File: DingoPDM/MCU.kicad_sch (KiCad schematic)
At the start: 39 parts, among them J4 SWD_10, SW3 SW_SPDT, U1 W25Q32JVSSIQ_TR, U11 STM32F303CCTx, U19 PCA82C250, U21 TLP172AM, Y1 8mHz, Y2 32.768kHz

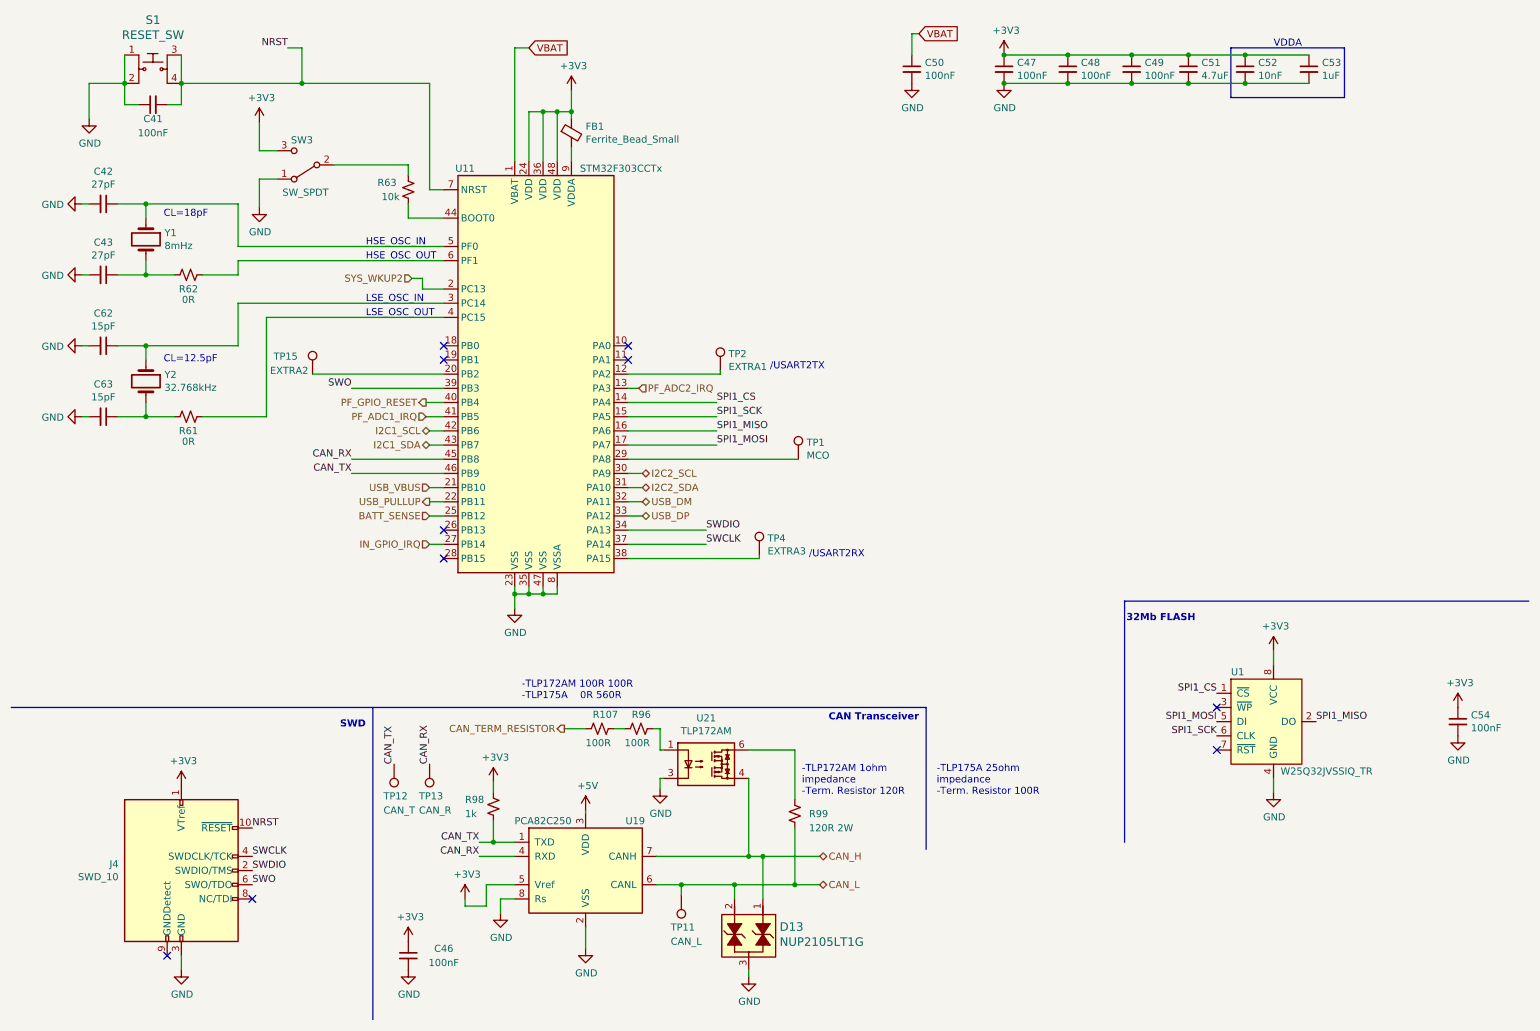
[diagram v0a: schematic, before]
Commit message: Swapped to AMPSEAL 14 pins
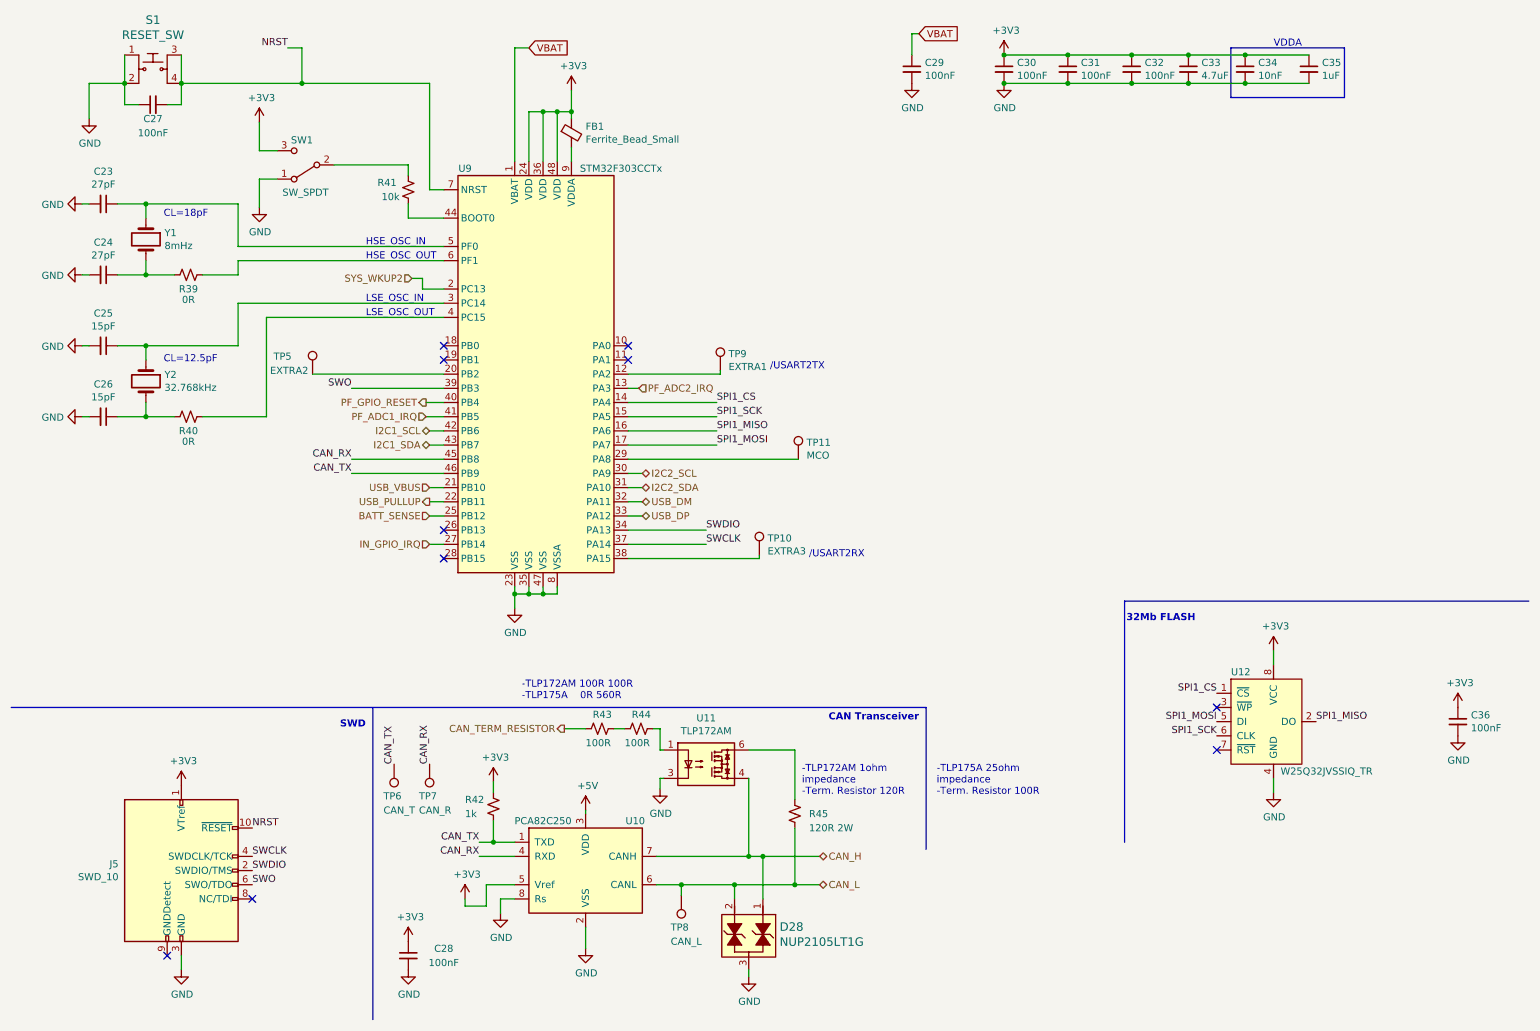
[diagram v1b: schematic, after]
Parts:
- renumbered C42 to C23, C43 to C24, C62 to C25, C63 to C26, C41 to C27, C46 to C28, C50 to C29, C47 to C30, C48 to C31, C49 to C32, C51 to C33, C52 to C34, C53 to C35, C54 to C36, D13 to D28, J4 to J5, R62 to R39, R61 to R40, R63 to R41, R98 to R42, R107 to R43, R96 to R44, R99 to R45, SW3 to SW1, TP4 to TP10, TP1 to TP11, TP15 to TP5, TP12 to TP6, TP13 to TP7, TP11 to TP8, TP2 to TP9, U19 to U10, U21 to U11, U1 to U12, U11 to U9

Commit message: Removed unused IRQs, added pd res on PF GPIO reset
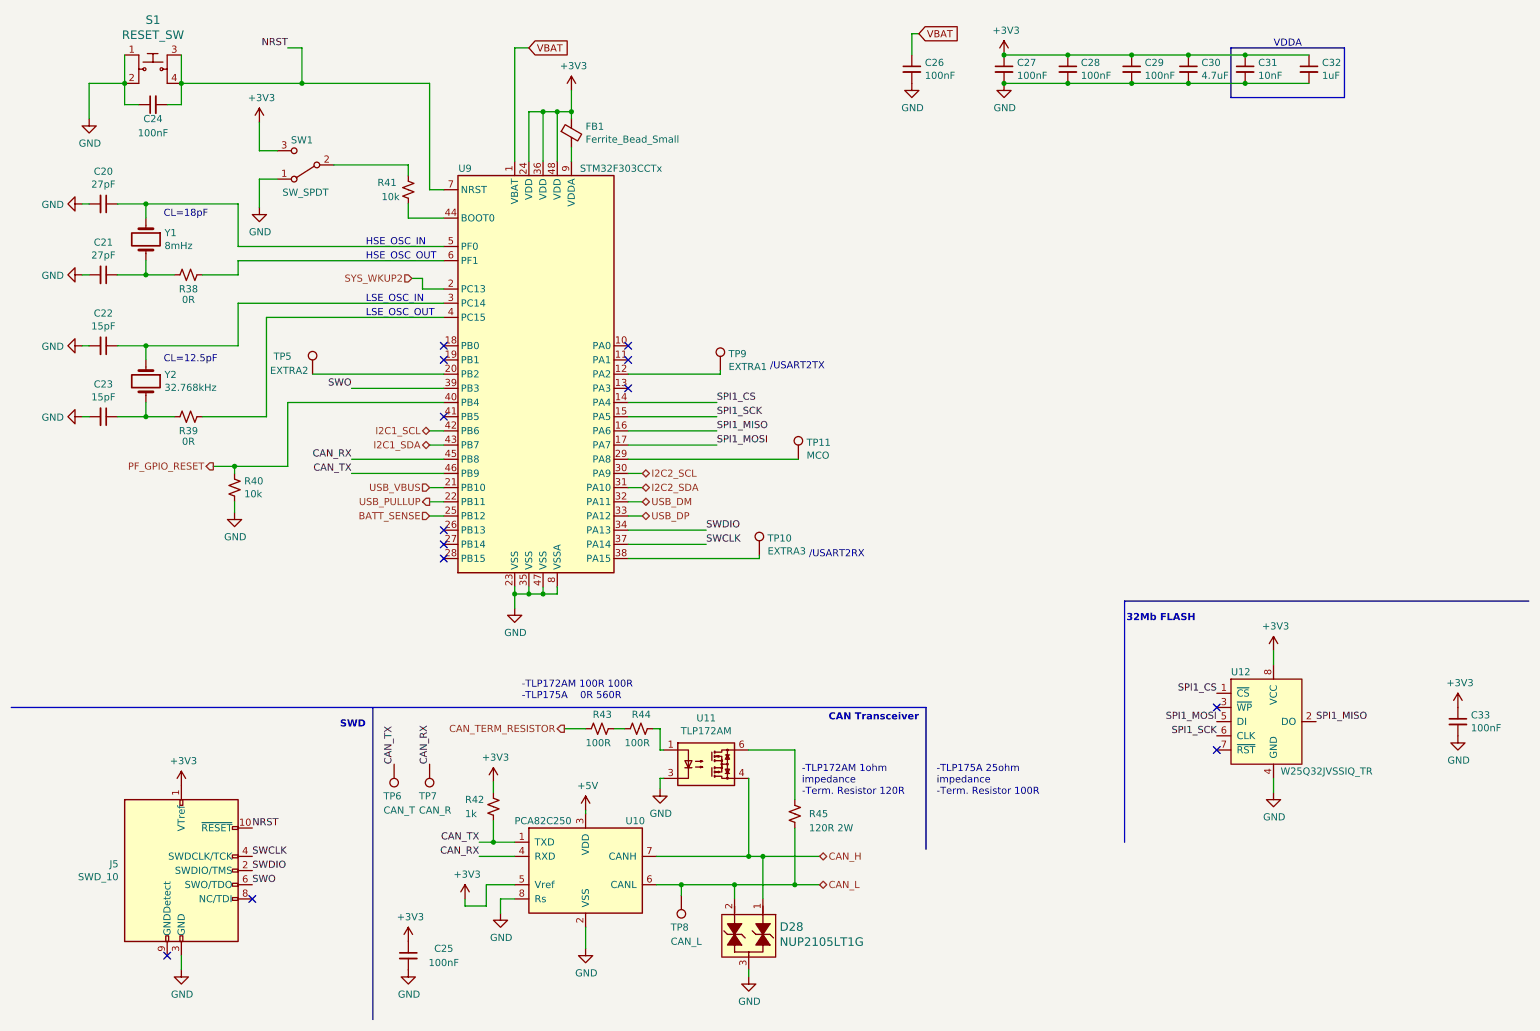
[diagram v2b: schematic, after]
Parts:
- added R40: 10k, Resistor_SMD:R_0805_2012Metric, symbol Device:R_Small_US
- renumbered C23 to C20, C24 to C21, C25 to C22, C26 to C23, C27 to C24, C28 to C25, C29 to C26, C30 to C27, C31 to C28, C32 to C29, C33 to C30, C34 to C31, C35 to C32, C36 to C33, R39 to R38, R40 to R39
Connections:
- net GND: now also R40.2
- net PF_GPIO_RESET: now also R40.1
- net IN_GPIO_IRQ: no longer names the net of U9.27 (PB14)
- net PF_ADC1_IRQ: no longer names the net of U9.41 (PB5)
- net PF_ADC2_IRQ: no longer names the net of U9.13 (PA3)
- no-connect marks 10 -> 13

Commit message: layout finished
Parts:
- removed TP8: CAN_L, TestPoint:TestPoint_Keystone_5000-5004_Miniature, symbol Connector:TestPoint
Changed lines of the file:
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@@
   (junction (at 233.68 24.13) (diameter 0) (color 0 0 0 0)
-  )
-  (junction (at 132.715 172.72) (diameter 0) (color 0 0 0 0)
   )
   (junction (at 105.41 120.65) (diameter 0) (color 0 0 0 0)
@@
     (stroke (width 0) (type default) (color 0 0 0 0))
   )
-  (wire (pts (xy 132.715 172.72) (xy 132.715 174.625))
-    (stroke (width 0) (type default) (color 0 0 0 0))
-  )
   (wire (pts (xy 113.03 35.56) (xy 113.03 34.29))
     (stroke (width 0) (type default) (color 0 0 0 0))
@@
     (stroke (width 0) (type default) (color 0 0 0 0))
   )
-  (wire (pts (xy 132.715 172.72) (xy 142.24 172.72))
-    (stroke (width 0) (type default) (color 0 0 0 0))
-  )
   (polyline (pts (xy 212.09 165.1) (xy 212.09 121.92))
     (stroke (width 0) (type default) (color 0 0 0 0))
@@
     (stroke (width 0) (type default) (color 0 0 0 0))
   )
-  (wire (pts (xy 128.27 172.72) (xy 132.715 172.72))
+  (wire (pts (xy 128.27 172.72) (xy 142.24 172.72))
     (stroke (width 0) (type default) (color 0 0 0 0))
   )
@@
     (pin "2")
   )
-  (symbol (lib_id "Connector:TestPoint") (at 132.715 174.625 180) (unit 1)
-    (in_bom yes) (on_board yes)
-    (property "Reference" "TP8" (id 0) (at 130.81 180.34 0)
-      (effects (font (size 1.27 1.27)) (justify right))
-    )
-    (property "Value" "CAN_L" (id 1) (at 130.81 182.88 0)
-      (effects (font (size 1.27 1.27)) (justify right))
-    )
-    (property "Footprint" "TestPoint:TestPoint_Keystone_5000-5004_Miniature" (id 2) (at 127.635 174.625 0)
-      (effects (font (size 1.27 1.27)) hide)
-    )
-    (property "Datasheet" "~" (id 3) (at 127.635 174.625 0)
-      (effects (font (size 1.27 1.27)) hide)
-    )
-    (pin "1")
-  )
   (symbol (lib_id "power:GND") (at 52.705 106.045 0) (unit 1)

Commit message: Moved folders
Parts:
- Y1: footprint Crystal:Crystal_SMD_5032-2Pin_5.0x3.2mm -> Crystals_Modify:Crystal_SMD_5032-2Pin_5.0x3.2mm_HandSoldering
- Y2: footprint Crystal:Crystal_SMD_3215-2Pin_3.2x1.5mm -> Crystals_Modify:Crystal_SMD_3215-2Pin_3.2x1.5mm_HandSoldering
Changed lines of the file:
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@@
       (effects (font (size 1.27 1.27)) (justify left))
     )
-    (property "Footprint" "Crystal:Crystal_SMD_5032-2Pin_5.0x3.2mm" (id 2) (at 36.83 57.15 0)
+    (property "Footprint" "Crystals_Modify:Crystal_SMD_5032-2Pin_5.0x3.2mm_HandSoldering" (id 2) (at 36.83 57.15 0)
       (effects (font (size 1.27 1.27)) hide)
     )
@@
       (effects (font (size 1.27 1.27)) (justify left))
     )
-    (property "Footprint" "Crystal:Crystal_SMD_3215-2Pin_3.2x1.5mm" (id 2) (at 36.83 82.55 0)
+    (property "Footprint" "Crystals_Modify:Crystal_SMD_3215-2Pin_3.2x1.5mm_HandSoldering" (id 2) (at 36.83 82.55 0)
       (effects (font (size 1.27 1.27)) hide)
     )

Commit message: Added export, fixed some PNs
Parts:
- R43, R44: Digi-Key_PN 311-560ARCT-ND -> 311-100CRCT-ND
- U10: Digi-Key_PN (none) -> 568-10316-1-ND
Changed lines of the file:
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@@
       (effects (font (size 1.27 1.27)) hide)
     )
-    (property "Digi-Key_PN" "" (id 4) (at 115.57 170.18 0)
+    (property "Digi-Key_PN" "568-10316-1-ND" (id 4) (at 115.57 170.18 0)
       (effects (font (size 1.27 1.27)) hide)
     )
@@
       (effects (font (size 1.27 1.27)) hide)
     )
-    (property "Digi-Key_PN" "311-560ARCT-ND" (id 4) (at 125.095 144.78 0)
+    (property "Digi-Key_PN" "311-100CRCT-ND" (id 4) (at 125.095 144.78 0)
       (effects (font (size 1.27 1.27)) hide)
     )
@@
       (effects (font (size 1.27 1.27)) hide)
     )
-    (property "Digi-Key_PN" "311-560ARCT-ND" (id 4) (at 118.11 144.78 0)
-      (effects (font (size 1.27 1.27)) hide)
-    )
+    (property "Digi-Key_PN" "311-100CRCT-ND" (id 4) (at 118.11 144.78 0)
+      (effects (font (size 1.27 1.27)) hide)
+    )

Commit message: V5 changes
Changed tracks/clearances/DRC to meet JLCPCB 2oz rules. Changed on switch to 12V input. Switched to TagConnect
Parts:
- removed J5: SWD_10, digikey-footprints:PinHeader_2x5_P1.27_SMD, symbol Connector:Conn_ARM_JTAG_SWD_10
- added J5: TC, Connector:Tag-Connect_TC2030-IDC-NL_2x03_P1.27mm_Vertical, symbol Connector:Conn_ARM_SWD_TagConnect_TC2030-NL
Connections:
- net +3V3: now also J5.1 (VCC)
- net GND: now also J5.5 (GND)
- net NRST: now also J5.3 (~{RESET})
- net SWCLK: now also J5.4 (SWCLK)
- net SWDIO: now also J5.2 (SWDIO)
- net SWO: now also J5.6 (SWO)
- no-connect marks 13 -> 11

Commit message: Documentation cleanup
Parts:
- D28: Category Circuit Protection -> (none); DK_Datasheet_Link http://www.onsemi.com/pub/Collateral/NUP2105L-D.PDF -> (none); DK_Detail_Page /product-detail/en/on-semiconductor/NUP2105LT1G/NUP2105LT1G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 -> (none); Family TVS - Diodes -> (none); MPN NUP2105LT1G -> (none); Manufacturer ON Semiconductor -> (none); Status Active -> (none)
- R45: Digi-Key_PN CRM2512-FX-1000ELFCT-ND -> A130710CT-ND
- S1: Category Switches -> (none); DK_Datasheet_Link https://www.te.com/commerce/DocumentDelivery/DDEController?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 -> (none); DK_Detail_Page /product-detail/en/te-connectivity-alcoswitch-switches/FSM4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 -> (none); Family Tactile Switches -> (none); MPN FSM4JSMATR -> (none); Manufacturer TE Connectivity ALCOSWITCH Switches -> (none); Status Active -> (none)
- U10: Mouser_PN 771-PCA82C250T/YM115 -> (none)
- U12: Category Integrated Circuits (ICs) -> (none); DK_Datasheet_Link http://www.winbond.com/resource-files/w25q32jv%20revg%20032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 -> (none); DK_Detail_Page /product-detail/en/winbond-electronics/W25Q32JVSSIQ-TR/W25Q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 -> (none); Family Memory -> (none); MPN W25Q32JVSSIQ TR -> (none); Manufacturer Winbond Electronics -> (none); Status Active -> (none)
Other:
- note removed: "-TLP172AM 100R 100R -TLP175A 0R 560R"

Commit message: V5 As Built
-Changed ADS1015 to MAX11613EUA+T due to supply issues
-Changed PCB to match JLCPCB 2oz rules
-Changed ON_SW input to 12V switched
-Switched to TagConnect TC2030
-Changed pin positions of GND, IN1, IN2
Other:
- title: (none) -> Dingo_PDM
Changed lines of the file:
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@@
 (kicad_sch (version 20230121) (generator eeschema)
   (paper "A4")
+  (title_block
+    (title "Dingo_PDM")
+    (date "2023-02-23")
+    (rev "v5")
+    (comment 3 "github.com/corygrant")
+    (comment 4 "Cory Grant")
+  )
   (junction (at 64.77 29.21) (diameter 0) (color 0 0 0 0)
   )
